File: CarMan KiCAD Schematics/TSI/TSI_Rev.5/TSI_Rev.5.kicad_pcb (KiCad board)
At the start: 2 copper layers, 203.2 x 165.1 mm, 252 parts, among them IC1 TS431ILT, IC4 TS431ILT, J1 J1, J10 J10, J11 J11, J12 J12, J13 Conn_01x01, J13.1 Conn_01x06, J13.2 Conn_01x06, J14 J14, J15 J15, J16 J16, J17 J17, J18 J18, J19 J19, J2 Current_Sensor, J20 J20, J21 J21, J22 J22, J23 Conn_01x01, J24 Conn_01x01, J25 Conn_01x01, J26 J26, J3 J3, J4 J4, J5 J5, J6 J6, J7 J7, J8 J8, J9 J9, K1 APAN3105, K2 G5LE-1-E, K3 SFS2-DC24V, K4 SFS2-DC24V, Q1 ZVP1320F, Q11 TN2130K1-G, Q2 MMBF170, Q3 ZVP1320F, Q5 SI1302DL-T1-E3, SW1 TS5A3159DBVT, U1 RDE03110S12, U10 MC7805BDTRKG, U11 TLP293, U12 REF3033, U13 TLP293, U14 MountingHole, U15 MountingHole, U16 TS372CDT, U17 Chassis Ground, U18 MCP6004, U19 74HC00, U2 MountingHole, U21 MCP6004, U22 MCP23016-I_SO, U23 DAC5574IDGS, U24 TLP293, U25 NCD9830DBR2G, U26 MCP6004, U29 SN74LVC1G08DCKR, U3 TS912, U30 TLP293, U31 TLP293, U32 TLP293, U34 TLP293, U35 MCP6004, U37 TLP293, U4 ACPL-C870, U40 MCP6004, U41 PDQ10-Q24-D5-D, U42 LT1763CS8-3.3PBF, U48 TLP293, U49 TLP293, U5 SI8600AB-B-IS, U6 TS912, U7 MCP6004, U8 74ACT11030, U9 STN3NF06L

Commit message: TSI (~97%)
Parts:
- removed TP2: APPS1_b, TestPoint:TestPoint_Pad_D3.0mm
- removed TP3: APPS2_b, TestPoint:TestPoint_Pad_D3.0mm
- removed TP9: APPS_DIFF, TestPoint:TestPoint_Pad_D3.0mm
- added APPS1_b1: APPS1_b, TestPoint:TestPoint_Pad_D3.0mm, F.Cu at (175.1, 81.9)
- added APPS2_b1: APPS2_b, TestPoint:TestPoint_Pad_D3.0mm, F.Cu at (180.3, 81.9)
- added APPS_DIFF1: APPS_DIFF, TestPoint:TestPoint_Pad_D3.0mm, F.Cu at (185.4, 81.9)
- added J21: J21, Connector_PinSocket_2.54mm:PinSocket_1x04_P2.54mm_Vertical, F.Cu at (218.2, 26.4)
- added J23: J23, Connector_PinSocket_2.54mm:PinSocket_1x02_P2.54mm_Vertical, F.Cu at (144.6, 60.9)
- added J29: J29, Connector_PinHeader_1.00mm:PinHeader_1x01_P1.00mm_Vertical, F.Cu at (141.7, 150.3)
- J19: footprint Connector_PinSocket_2.54mm:PinSocket_1x08_P2.54mm_Vertical -> Connector_PinSocket_2.54mm:PinSocket_1x04_P2.54mm_Vertical
- J22: renamed from J21; value J21 -> J22
- J27: renamed from J22; value J22 -> J27
- TP5: value PC_Ready -> PC_Ready_HV
- U14: value MountingHole -> Bottom Left
- U15: value MountingHole -> Top Left
- U17: value Chassis Ground -> Top Right
- U2: value MountingHole -> Bottom Right
- moved TSAL_RTN1 117.0 mm to (162.9, 141.3)
- moved APPS1_ISO1 53.9 mm to (190.5, 81.9)
- moved TP5 17.7 mm to (274.6, 216.7)
- moved TP8 17.7 mm to (260.4, 216.7)
- moved TP4 17.7 mm to (267.5, 215.7)
- moved TP6 17.7 mm to (255.1, 216.5)
- moved J19 10.2 mm to (171.1, 92.0)
- moved R17 4.94 mm to (179.9, 65.4)
- moved TP7 4.28 mm to (168.1, 141.3)
- moved R35 3.12 mm to (235.0, 56.8), turned to 0 degrees
- moved D2 2.18 mm to (178.1, 68.7)
- moved R18 2.18 mm to (183.5, 68.1)
- moved U2 1.99 mm to (335.4, 201.2)
- moved U14 1.97 mm to (147.7, 201.2)
- moved C10 1.80 mm to (170.1, 70.7)
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- renumbered TP1 to APPS1_ISO1, J23 to J28
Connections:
- J19 pad 1: /SDA -> /PC_Ready
- J19 pad 2: /SCL -> /SL1_In
- J19 pad 3: /PC_Ready -> /IMD_Status
- J19 pad 4: /SL1_In -> /Throttle_SEL
- R54 pad 2: /IGNI_VCC -> /PCDC_Circuit/PC_Ready_HV
- TP5 pad 1: /PCDC_Circuit/Precharge_Ready -> /PCDC_Circuit/PC_Ready_HV
- U29 pad 1: /PCDC_Circuit/Precharge_Ready -> /PCDC_Circuit/PC_Ready_HV
- U40 pad 7: /PCDC_Circuit/Precharge_Ready -> /PCDC_Circuit/PC_Ready_HV
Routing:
- net /TSI-TP/APPS1_ISO: track 28.6 -> 64.2 mm, vias 0 -> 2
- net /PC_Ready: track 188.2 -> 219.6 mm
- net /TSI-TP/APPS_DIFF: track 105.1 -> 135.0 mm, vias 2 -> 4
- net /TSI-TP/APPS1_b: track 35.0 -> 62.3 mm, vias 0 -> 2
- net /TSI-TP/APPS2_b: track 76.0 -> 100.7 mm, vias 5 -> 7
- net /SCL: track 247.7 -> 270.7 mm, vias 10 -> 12
- net /AIRS-: track 1462.0 -> 1483.2 mm, vias 42 -> 37
- net /SDA: track 286.1 -> 302.6 mm, vias 11 -> 9
- net /PCDC_Circuit/Precharge_Ready: track 12.2 -> 0.00 mm, vias 2 -> 0
- net /PCDC_Circuit/PC_Ready_HV: track 0.00 -> 12.2 mm, vias 0 -> 2
- net Net-(D2-Pad8): track 9.78 -> 4.31 mm
- net /TSI-TP/U8_Pin9: track 58.1 -> 54.8 mm
- net /5V_ISO_RTN: track 251.8 -> 254.8 mm
- net /10V: track 300.5 -> 298.4 mm, vias 14 -> 10
- net /APPS2: track 53.3 -> 51.6 mm
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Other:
- board text added: "LV RTN"

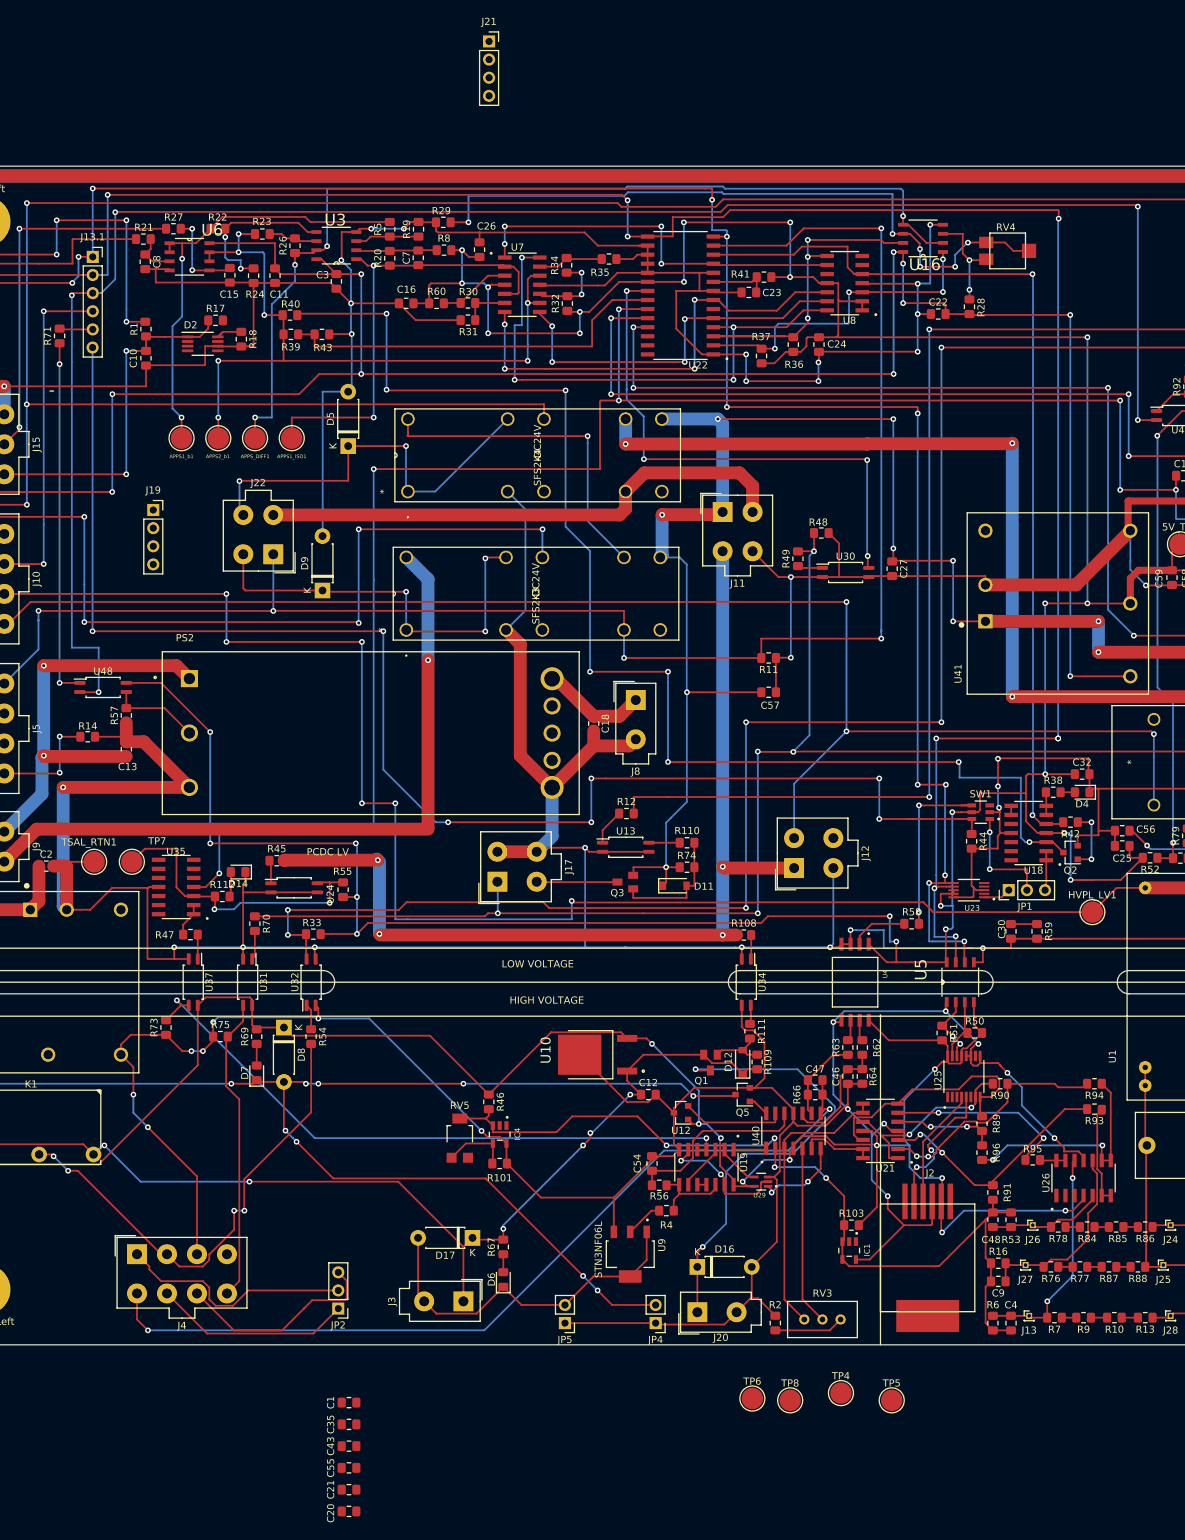
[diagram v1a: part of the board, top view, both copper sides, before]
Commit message: TSI (~98%) - Added right side testing connector - Finish left side testing connector - Added Caps to HV side
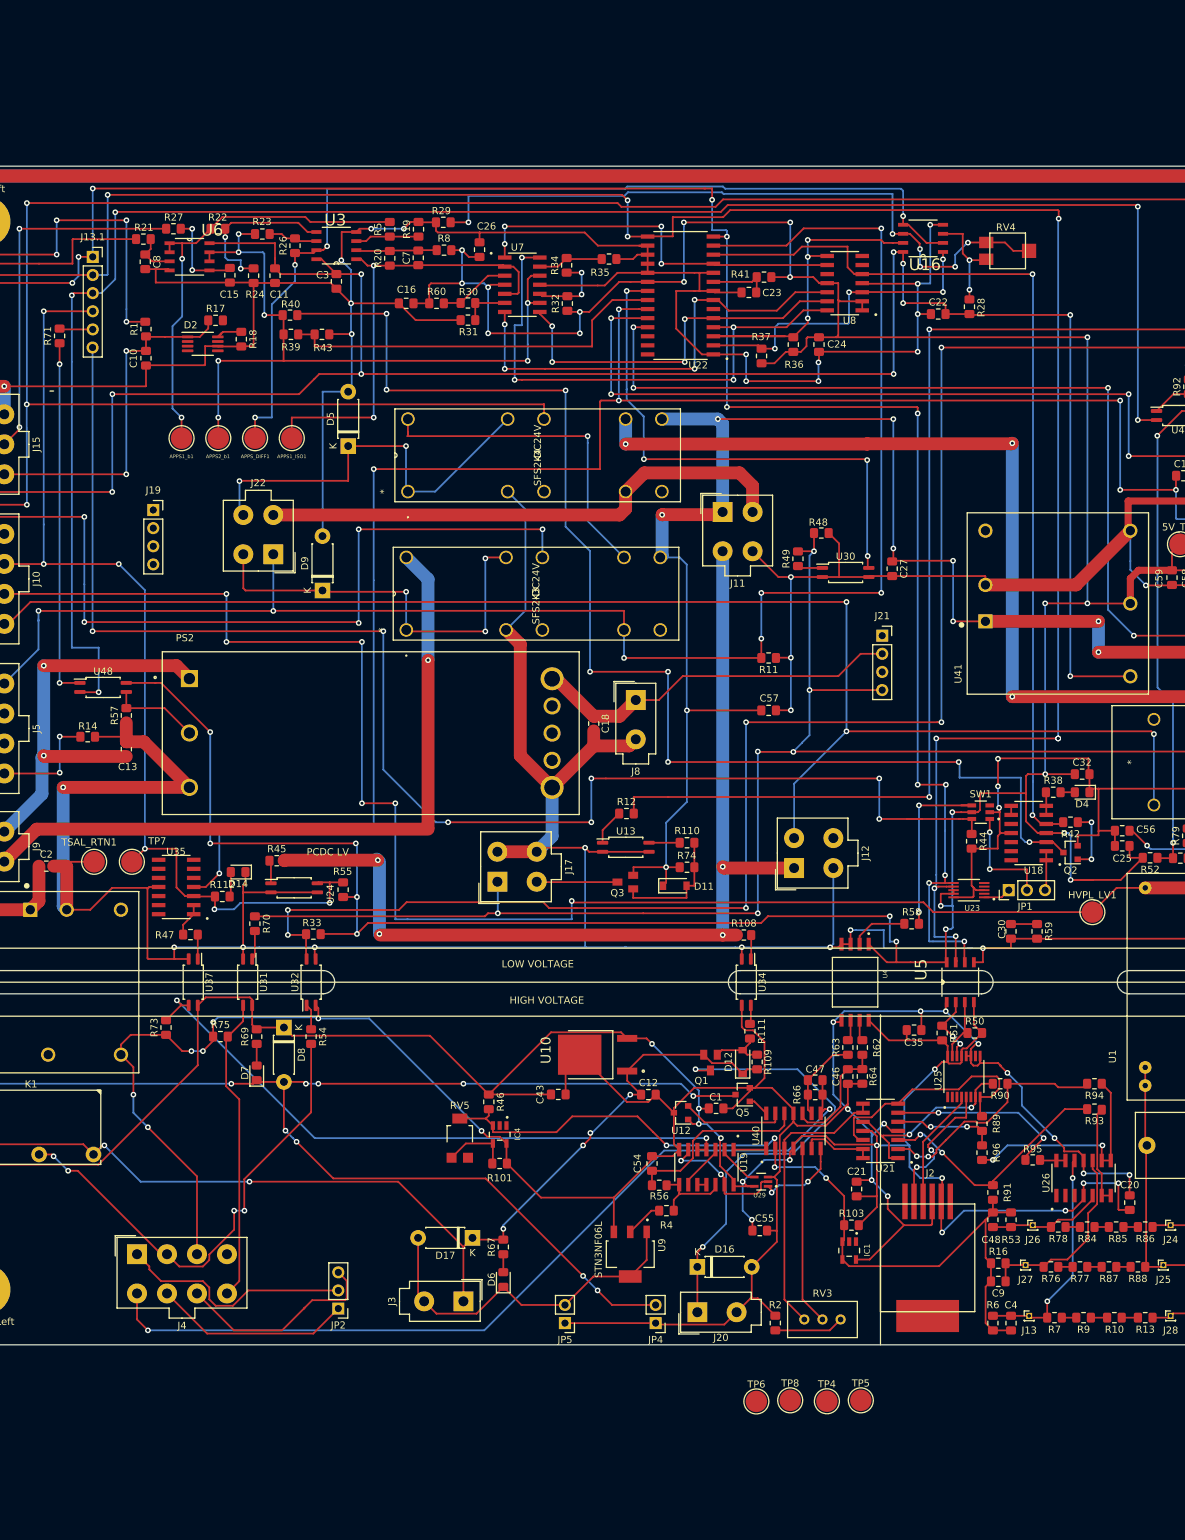
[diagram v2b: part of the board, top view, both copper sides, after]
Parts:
- moved C20 117.6 mm to (307.9, 189.0), turned to 90 degrees
- moved J21 99.8 mm to (273.3, 109.6)
- moved C35 96.5 mm to (277.7, 164.8)
- moved C21 82.6 mm to (269.7, 187.1), turned to 90 degrees
- moved C55 66.4 mm to (256.1, 192.9)
- moved C1 65.9 mm to (250.0, 175.8)
- moved C43 57.3 mm to (227.9, 173.9)
- moved TP5 4.33 mm to (270.3, 216.7)
- moved C57 2.54 mm to (257.3, 120.1)
- moved TP4 2.28 mm to (265.5, 216.8)
- moved TP6 0.69 mm to (255.6, 216.9)
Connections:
- J19 pad 1: /PC_Ready -> Net-(J19-Pad1)
- J21 pad 1: Net-(J21-Pad1) -> /Drive_BTN
- J21 pad 2: Net-(J21-Pad2) -> /12V_Cooling
- J21 pad 3: Net-(J21-Pad3) -> /BOT_Out
- J21 pad 4: Net-(J21-Pad4) -> /Brake_Light
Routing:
- net /Safety_Loop: track 91.1 -> 143.0 mm, vias 4 -> 6
- net /12V_Cooling: track 14.8 -> 52.0 mm
- net /5HV: track 279.1 -> 312.9 mm, vias 10 -> 14
- net /DC_RELAY-: track 381.9 -> 411.0 mm, vias 15 -> 19
- net /Brake_Light: track 214.0 -> 224.2 mm, vias 5 -> 6
- net /AIRS-: track 1483.2 -> 1487.7 mm, vias 37 -> 38
- net /IMD_Status: track 230.0 -> 229.7 mm, vias 5 -> 7

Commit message: TSI (~98.5%)
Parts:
- TP7: value SL_TP -> Safety_Loop
- moved TP5 28.0 mm to (264.6, 189.3)
- moved TP8 7.09 mm to (267.4, 215.6)
- moved TP4 3.48 mm to (262.3, 215.4)
- moved J19 2.44 mm to (172.8, 90.2)
- moved TP6 2.28 mm to (257.4, 215.4)
- moved R49 1.08 mm to (260.4, 98.7)
- renumbered APPS1_ISO1 to TP1, 5V_TP1 to TP10, 3.3V_TP1 to TP11, HVPL_LV1 to TP12, TSAL_RTN1 to TP14, APPS_DIFF1 to TP2, APPS1_b1 to TP3, APPS2_b1 to TP9
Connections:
- J19 pad 1: Net-(J19-Pad1) -> /SL1_In
- J19 pad 2: /SL1_In -> /TSAL
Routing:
- net /Drive_BTN: track 11.7 -> 104.6 mm, vias 0 -> 6
- net /BOT_Out: track 22.6 -> 84.9 mm, vias 1 -> 5
- net /SL1_In: track 100.4 -> 142.6 mm, vias 1 -> 3
- net /IMD_Status: track 229.7 -> 246.2 mm, vias 7 -> 8
- net /TSAL: track 256.5 -> 270.7 mm, vias 6 -> 8
- net /Throttle_SEL: track 201.3 -> 211.5 mm, vias 7 -> 8
- net /PCDC_Circuit/PC_Ready_HV: track 12.2 -> 16.2 mm
- net /AIRS-: track 1487.7 -> 1485.8 mm, vias 38 -> 37
- net Net-(R49-Pad1): track 3.53 -> 4.65 mm
